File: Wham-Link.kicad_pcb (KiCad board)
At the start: 2 copper layers, 5 parts, among them U1 W5500, U2 AMS1117-3.3, U3 AP2112K-3.3TRG1, U4 ESP32-WROOM-32UE

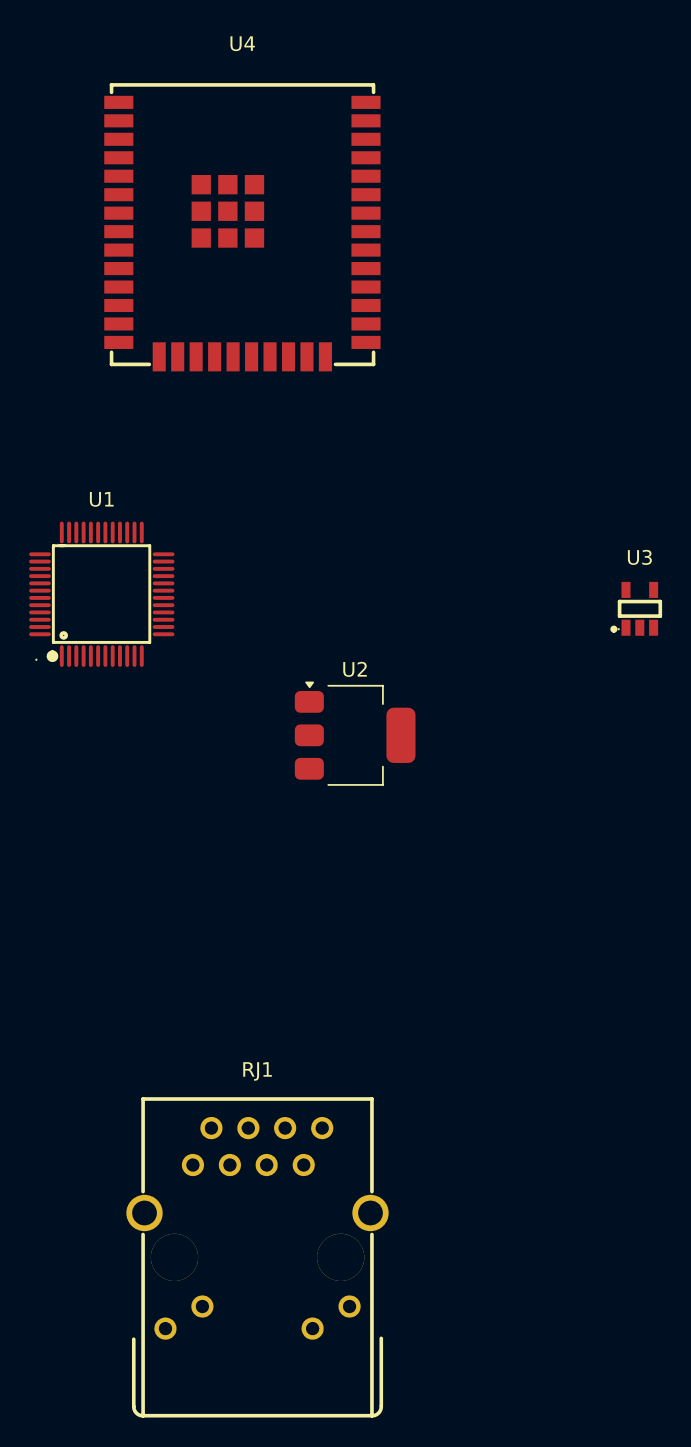
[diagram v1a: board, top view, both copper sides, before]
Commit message: PHY <-> Ethernet schematic touchups
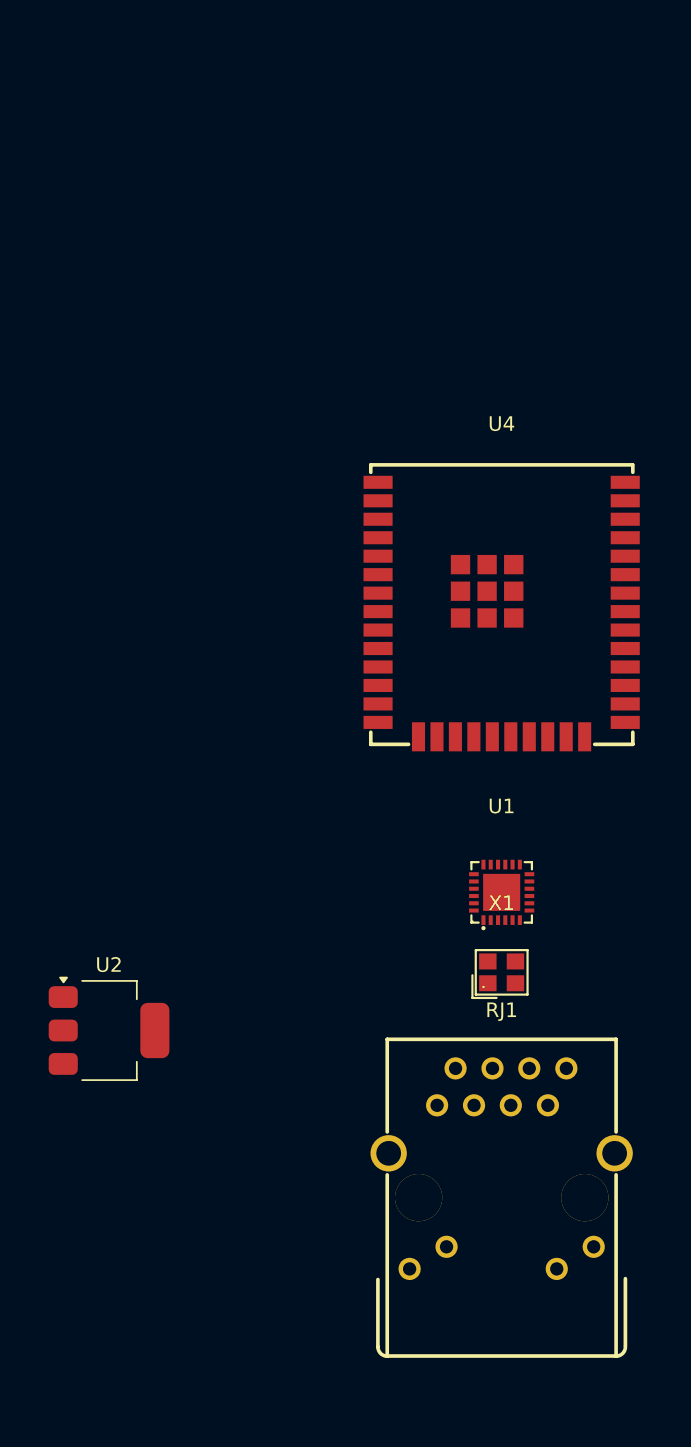
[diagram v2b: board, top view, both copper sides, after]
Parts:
- removed U3: AP2112K-3.3TRG1, imported-project-library:SOT-25-5_L2.9-W1.6-P0.95-LS2.8-BL
- added X1: ECS-2520MV-250-CN-TR, imported-project-library:OSC-SMD_4P-L2.5-W2.0-BL, F.Cu at (162.0, 119.0)
- U1: value W5500 -> LAN8720A-CP-TR; footprint imported-project-library:LQFP-48_L7.0-W7.0-P0.50-LS9.0-BL -> imported-project-library:QFN-24_L4.0-W4.0-P0.50-BL-EP2.6
- moved U1 34.3 mm to (162.0, 113.5)
- moved U4 31.6 mm to (162.0, 94.0)
- moved U2 26.4 mm to (135.0, 123.0)
- moved RJ1 17.3 mm to (162.0, 132.5)
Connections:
- RJ1 pad 1: unconnected-(RJ1-Pad1) -> Net-(U1-TXP)
- RJ1 pad 10: unconnected-(RJ1-LLED--Pad10) -> Net-(RJ1-LLED-)
- RJ1 pad 11: unconnected-(RJ1-RLED+-Pad11) -> VDD1A
- RJ1 pad 12: unconnected-(RJ1-RLED--Pad12) -> Net-(RJ1-RLED-)
- RJ1 pad 13: unconnected-(RJ1-GND-Pad13) -> VDD1A
- RJ1 pad 14: unconnected-(RJ1-GND-Pad14) -> VDD1A
- RJ1 pad 2: unconnected-(RJ1-Pad2) -> Net-(U1-TXN)
- RJ1 pad 3: unconnected-(RJ1-Pad3) -> Net-(U1-RXP)
- RJ1 pad 4: unconnected-(RJ1-Pad4) -> VDDA
- RJ1 pad 5: unconnected-(RJ1-Pad5) -> VDDA
- RJ1 pad 6: unconnected-(RJ1-Pad6) -> Net-(U1-RXN)
- RJ1 pad 7: unconnected-(RJ1-Pad7) -> Net-(R3-Pad2)
- RJ1 pad 8: unconnected-(RJ1-Pad8) -> Net-(R3-Pad2)
- RJ1 pad 9: unconnected-(RJ1-LLED+-Pad9) -> VDD1A
- U1 pad 1: unconnected-(U1-TXN-Pad1) -> VDD1A
- U1 pad 11: unconnected-(U1-AVDD-Pad11) -> IO27
- U1 pad 12: unconnected-(U1-NC-Pad12) -> IO18
- U1 pad 13: unconnected-(U1-NC-Pad13) -> IO23
- U1 pad 14: unconnected-(U1-AGND-Pad14) -> IO0
- U1 pad 15: unconnected-(U1-AVDD-Pad15) -> IO5
- U1 pad 16: unconnected-(U1-AGND-Pad16) -> IO21
- U1 pad 17: unconnected-(U1-AVDD-Pad17) -> IO19
- U1 pad 18: unconnected-(U1-VBG-Pad18) -> IO22
- U1 pad 19: unconnected-(U1-AGND-Pad19) -> VDD1A
- U1 pad 2: unconnected-(U1-TXP-Pad2) -> LED2
- U1 pad 20: unconnected-(U1-TOCAP-Pad20) -> Net-(U1-TXN)
- U1 pad 21: unconnected-(U1-AVDD-Pad21) -> Net-(U1-TXP)
- U1 pad 22: unconnected-(U1-1V2O-Pad22) -> Net-(U1-RXN)
- U1 pad 23: unconnected-(U1-RSVD-Pad23) -> Net-(U1-RXP)
- U1 pad 3: unconnected-(U1-AGND-Pad3) -> LED1
- U1 pad 5: unconnected-(U1-RXN-Pad5) -> CLKIN
- U1 pad 6: unconnected-(U1-RXP-Pad6) -> VDDCR
- U1 pad 7: unconnected-(U1-DNC-Pad7) -> IO26
- U1 pad 8: unconnected-(U1-AVDD-Pad8) -> IO25
- U1 pad 9: unconnected-(U1-AGND-Pad9) -> VDD1A
- U2 pad 1: +3V3 -> VDD1A
- U2 pad 2: +3V3 -> VDD1A
- U4 pad 10: unconnected-(U4-IO25-Pad10) -> IO25
- U4 pad 11: unconnected-(U4-IO26-Pad11) -> IO26
- U4 pad 12: unconnected-(U4-IO27-Pad12) -> IO27
- U4 pad 25: unconnected-(U4-IO0-Pad25) -> IO0
- U4 pad 29: unconnected-(U4-IO5-Pad29) -> IO5
- U4 pad 30: unconnected-(U4-IO18-Pad30) -> IO18
- U4 pad 31: unconnected-(U4-IO19-Pad31) -> IO19
- U4 pad 33: unconnected-(U4-IO21-Pad33) -> IO21
- U4 pad 36: unconnected-(U4-IO22-Pad36) -> IO22
- U4 pad 37: unconnected-(U4-IO23-Pad37) -> IO23
